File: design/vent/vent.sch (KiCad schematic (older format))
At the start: 12 parts, among them J1 Conn_01x02, J2 SDA_TEST, J3 RX_TEST, J4 TX_TEST, J5 SCL_TEST, J6 SCK_TEST, J7 MISO_TEST, J8 MOSI_TEST, J9 CS_TEST

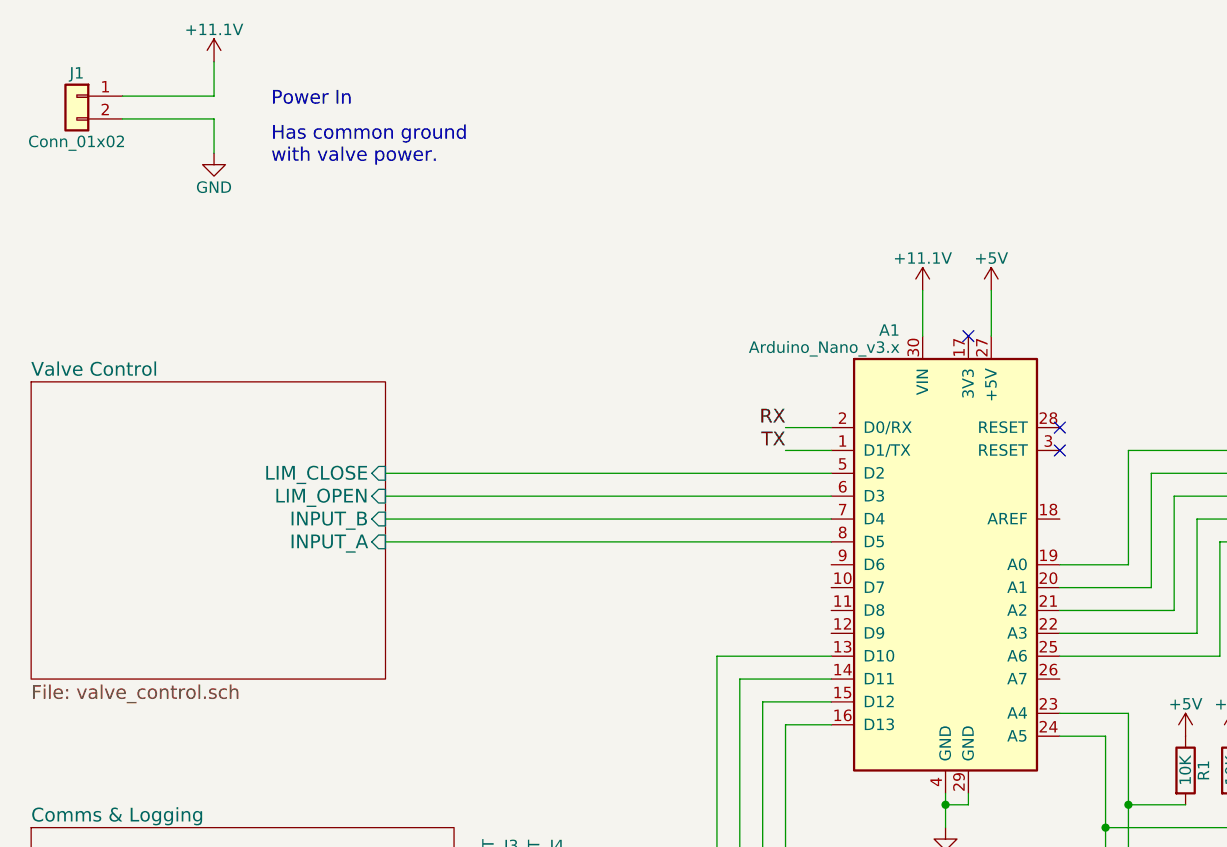
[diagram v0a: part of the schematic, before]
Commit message: Refine schematic
- Add part numbers and correct pinout for mosfets
- Add fuses to battery inputs
- Add decoupling caps to logic translators
- Add flyback diodes to H Bridge, to be populated if the body diodes of
  the mosfets are not sufficient.
- Change H Bridge to operate with 4 inputs instead of 2.

Also, misc directory cleanup.
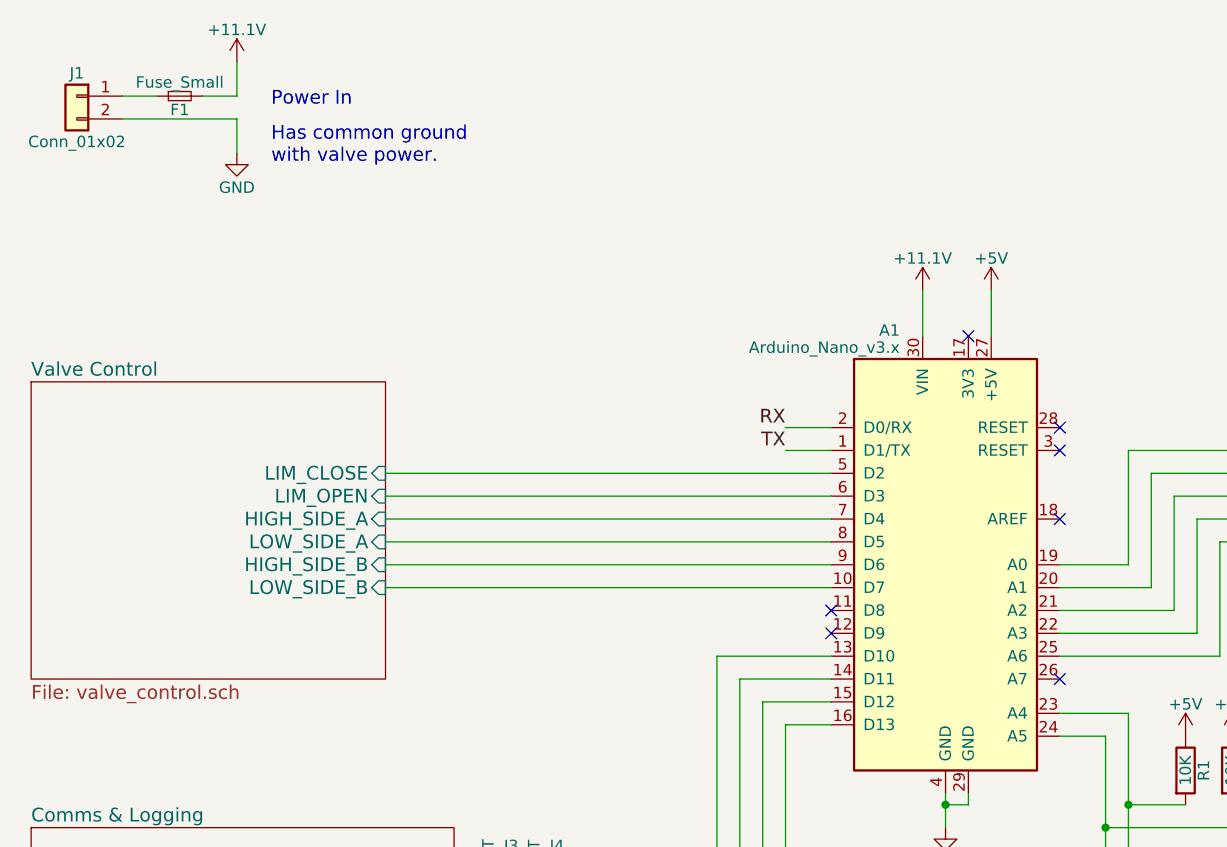
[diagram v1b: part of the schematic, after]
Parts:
- added F1: Fuse_Small, symbol Fuse_Small
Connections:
- net +11.1V: now also F1.2; no longer J1.1 (Pin_1)
- net Valve Control/LOW_SIDE_B: now reaches A1.10 (D7)
- net Valve Control/HIGH_SIDE_B: now reaches A1.9 (D6)
- net Valve Control/INPUT_A renamed Valve Control/LOW_SIDE_A
- net Valve Control/INPUT_B renamed Valve Control/HIGH_SIDE_A
- new net: F1.1, J1.1 (Pin_1)
- no-connect marks 3 -> 7
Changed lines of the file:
@@
 L +11.1V #PWR1
 U 1 1 5ADF8011
-P 2400 1700
-F 0 "#PWR1" H 2400 1550 50  0001 C CNN
-F 1 "+11.1V" H 2400 1840 50  0000 C CNN
-F 2 "" H 2400 1700 50  0001 C CNN
-F 3 "" H 2400 1700 50  0001 C CNN
-	1    2400 1700
+P 2500 1700
+F 0 "#PWR1" H 2500 1550 50  0001 C CNN
+F 1 "+11.1V" H 2500 1840 50  0000 C CNN
+F 2 "" H 2500 1700 50  0001 C CNN
+F 3 "" H 2500 1700 50  0001 C CNN
+	1    2500 1700
 	1    0    0    -1
 $EndComp
@@
 L GND #PWR2
 U 1 1 5ADF8038
-P 2400 2100
-F 0 "#PWR2" H 2400 1850 50  0001 C CNN
-F 1 "GND" H 2400 1950 50  0000 C CNN
-F 2 "" H 2400 2100 50  0001 C CNN
-F 3 "" H 2400 2100 50  0001 C CNN
-	1    2400 2100
+P 2500 2100
+F 0 "#PWR2" H 2500 1850 50  0001 C CNN
+F 1 "GND" H 2500 1950 50  0000 C CNN
+F 2 "" H 2500 2100 50  0001 C CNN
+F 3 "" H 2500 2100 50  0001 C CNN
+	1    2500 2100
 	1    0    0    -1
 $EndComp
@@
 F0 "Valve Control" 60
 F1 "valve_control.sch" 60
-F2 "INPUT_A" I R 3150 3800 60
-F3 "INPUT_B" I R 3150 3700 60
-F4 "LIM_OPEN" I R 3150 3600 60
-F5 "LIM_CLOSE" I R 3150 3500 60
+F2 "LIM_OPEN" I R 3150 3600 60
+F3 "LIM_CLOSE" I R 3150 3500 60
+F4 "HIGH_SIDE_A" I R 3150 3700 60
+F5 "LOW_SIDE_A" I R 3150 3800 60
+F6 "HIGH_SIDE_B" I R 3150 3900 60
+F7 "LOW_SIDE_B" I R 3150 4000 60
 $EndSheet
 $Comp
@@
 	4900 4600 5100 4600
 Wire Wire Line
-	2400 1700 2400 1850
-Wire Wire Line
-	2400 1850 2000 1850
-Wire Wire Line
-	2400 2100 2400 1950
-Wire Wire Line
-	2400 1950 2000 1950
+	2500 1700 2500 1850
+Wire Wire Line
+	2500 1950 2500 2100
+Wire Wire Line
+	2000 1950 2500 1950
 Wire Wire Line
 	5500 2900 5500 2700
@@
 Wire Wire Line
 	3150 3600 5100 3600
-Wire Wire Line
-	3150 3700 5100 3700
-Wire Wire Line
-	3150 3800 5100 3800
 Wire Wire Line
 	7150 5700 7150 5550
@@
 	3900 5400 3900 5600
 Connection ~ 3900 5600
+$Comp
+L Fuse_Small F1
+U 1 1 5AE9CD78
+P 2250 1850
+F 0 "F1" H 2250 1790 50  0000 C CNN
+F 1 "Fuse_Small" H 2250 1910 50  0000 C CNN
+F 2 "" H 2250 1850 50  0001 C CNN
+F 3 "" H 2250 1850 50  0001 C CNN
+	1    2250 1850
+	1    0    0    -1
+$EndComp
+Wire Wire Line
+	2000 1850 2150 1850
+Wire Wire Line
+	2500 1850 2350 1850
+Wire Wire Line
+	3150 3700 5100 3700
+Wire Wire Line
+	3150 3800 5100 3800
+Wire Wire Line
+	3150 3900 5100 3900
+Wire Wire Line
+	3150 4000 5100 4000
+NoConn ~ 5100 4100
+NoConn ~ 5100 4200
+NoConn ~ 6100 4400
+NoConn ~ 6100 3700
 $EndSCHEMATC

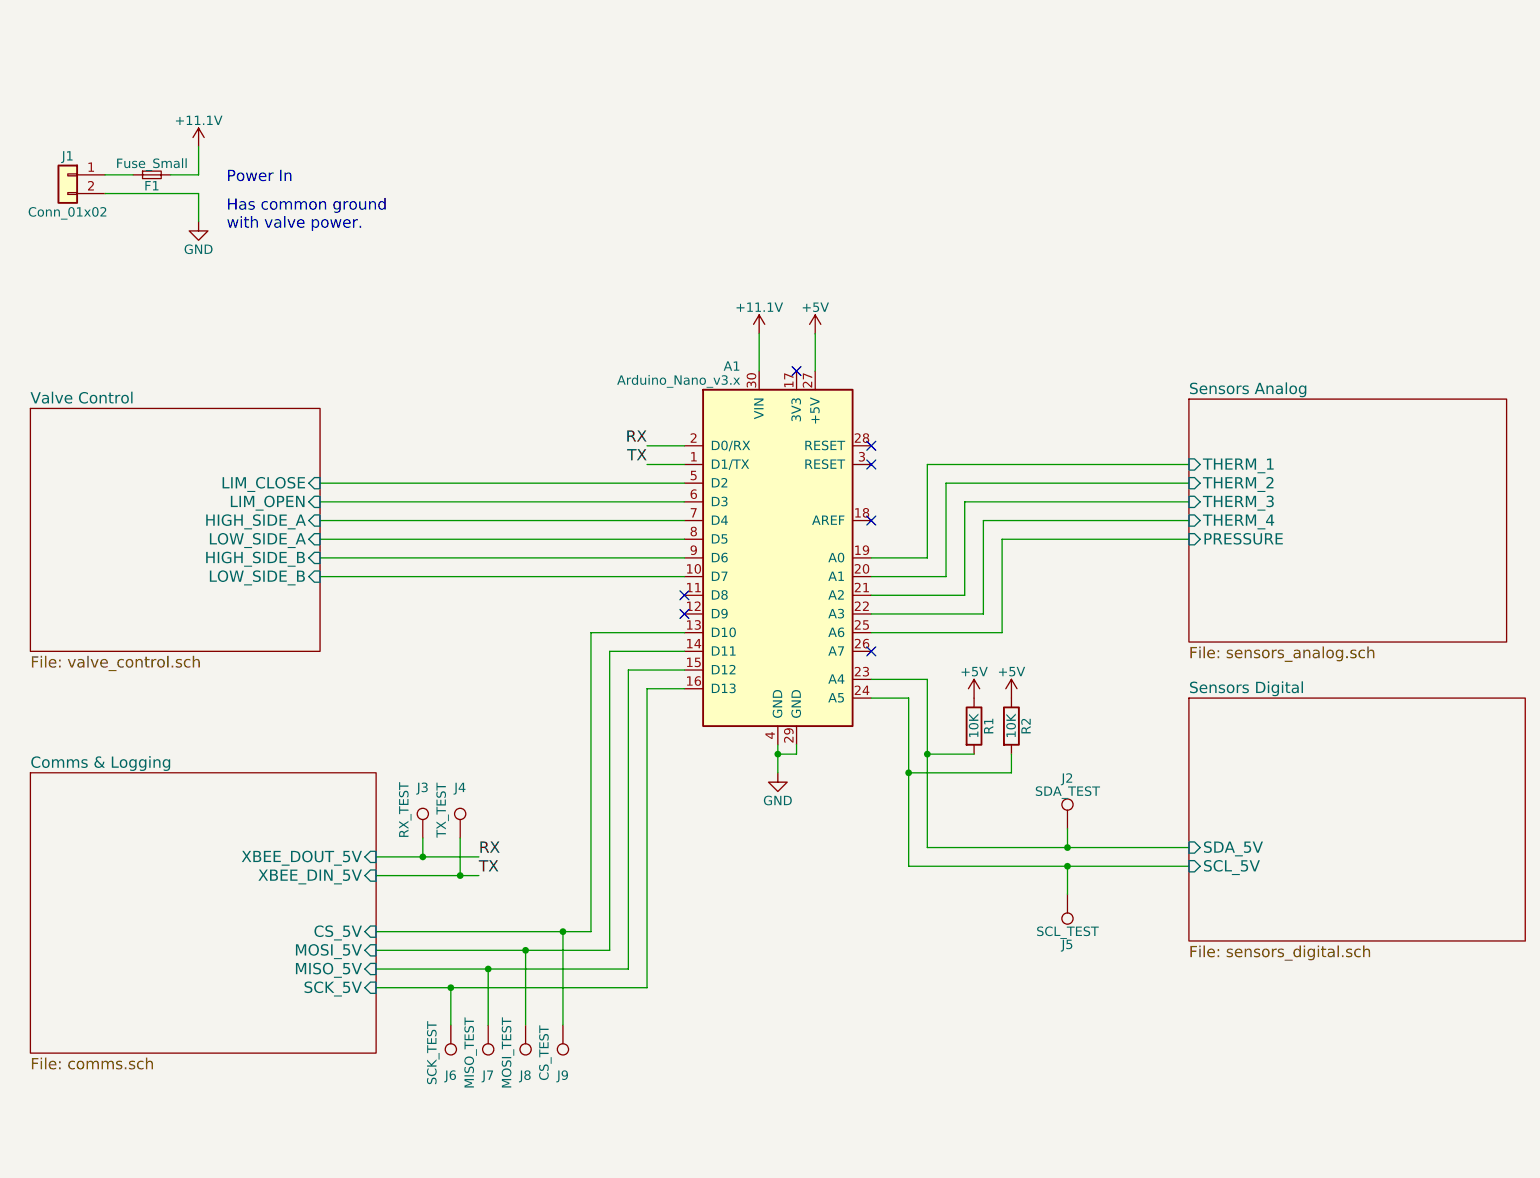
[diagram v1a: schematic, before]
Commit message: Review changes
- Add debug LEDs
- Add pullup resistors on logic shifters for xbee and sd card.
- Add 0 ohm resistor between valve and control power sources (to allow
  for either one of both sources to be used).
- Add another IMU
- Add gate resistors to valve control mosfets
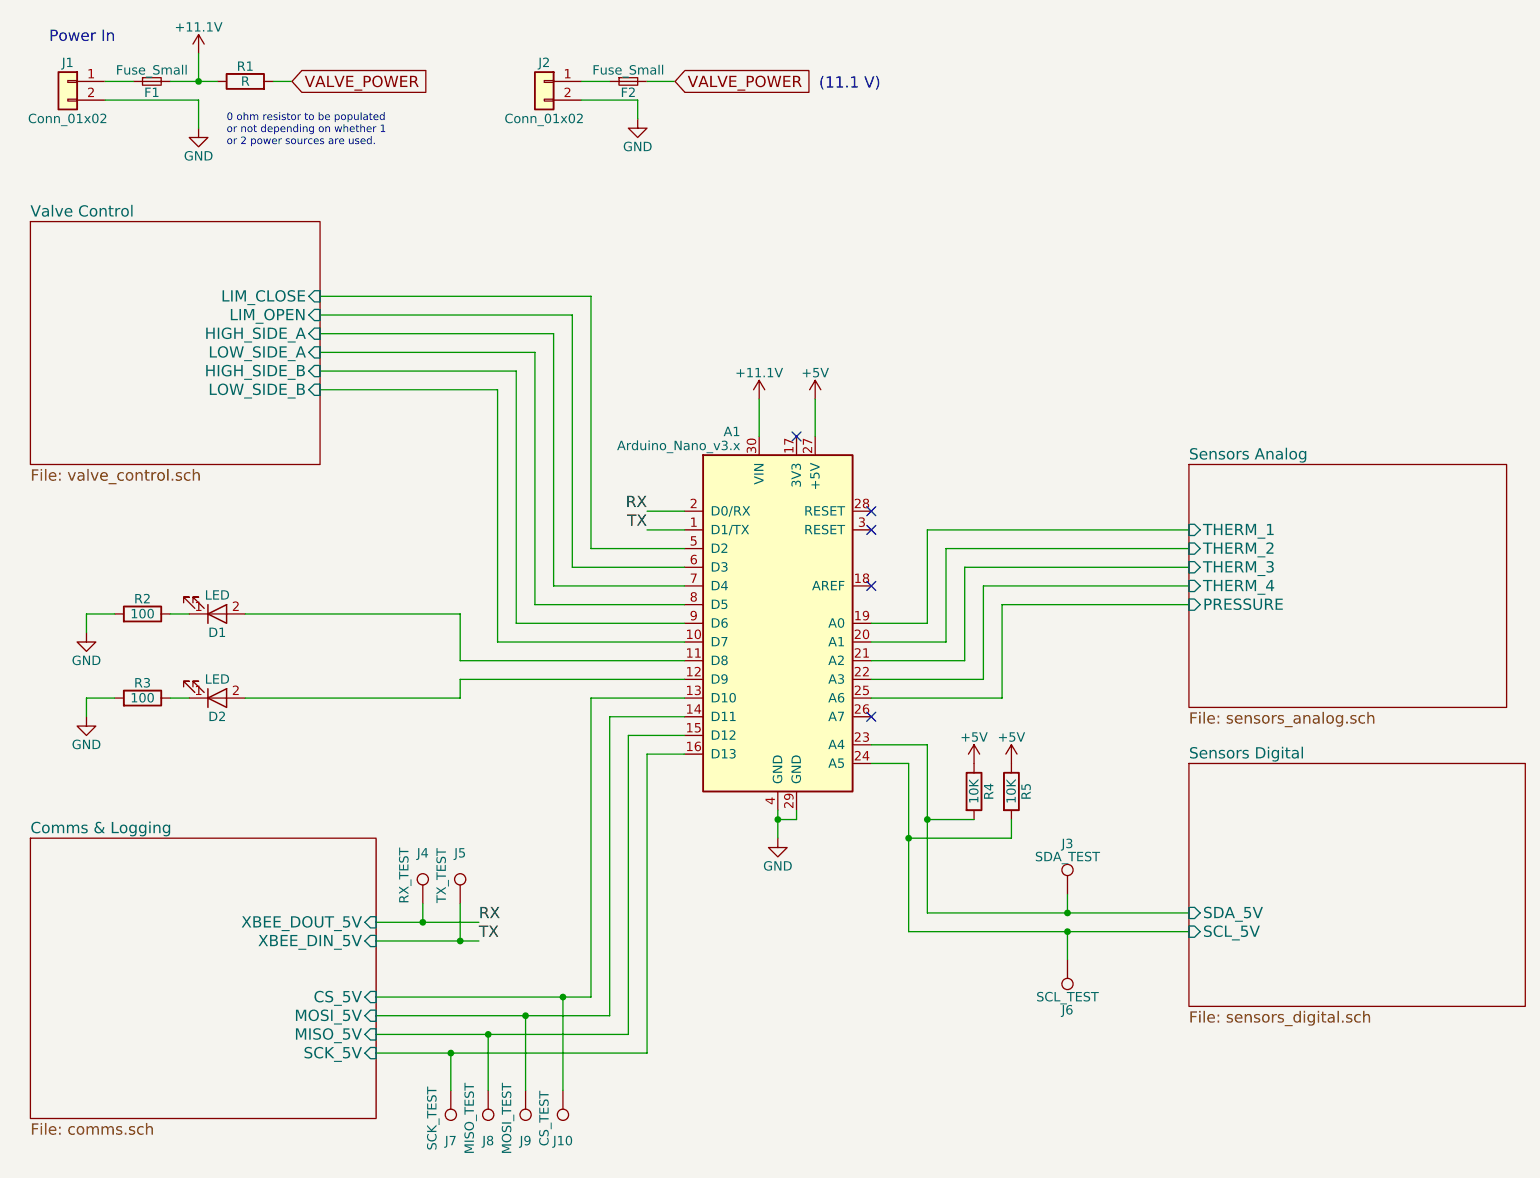
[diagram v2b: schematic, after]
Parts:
- added D1, D2: LED, symbol LED
- added F2: Fuse_Small, symbol Fuse_Small
- added J2: Conn_01x02, symbol Conn_01x02
- added R1: R, symbol R
- added R2, R3: 100, symbol R
- renumbered J9 to J10, J2 to J3, J3 to J4, J4 to J5, J5 to J6, J6 to J7, J7 to J8, J8 to J9, R1 to R4, R2 to R5
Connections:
- net +11.1V: now also R1.1
- net GND: now also J2.2 (Pin_2), R2.2, R3.2
- net at A1.11 (D8): now also D1.2 (A)
- net at A1.12 (D9): now also D2.2 (A)
- new net: D1.1 (K), R2.1
- new net: D2.1 (K), R3.1
- new net: F2.1, J2.1 (Pin_1)
- new net VALVE_POWER: F2.2, R1.2
- no-connect marks 7 -> 5
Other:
- note added: "(11.1 V)"
- note added: "0 ohm resistor to be populated\nor not depending on whether 1\nor 2 power sources are used."
- note removed: "Has common ground\nwith valve power."
- moved on the sheet: A1, F1, J1, J10, J3, J4, J5, J6, J7, J8, J9, R4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
